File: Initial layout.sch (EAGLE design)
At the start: 53 parts, among them J1 502585-0470, U2 TPS54540DDARQ1

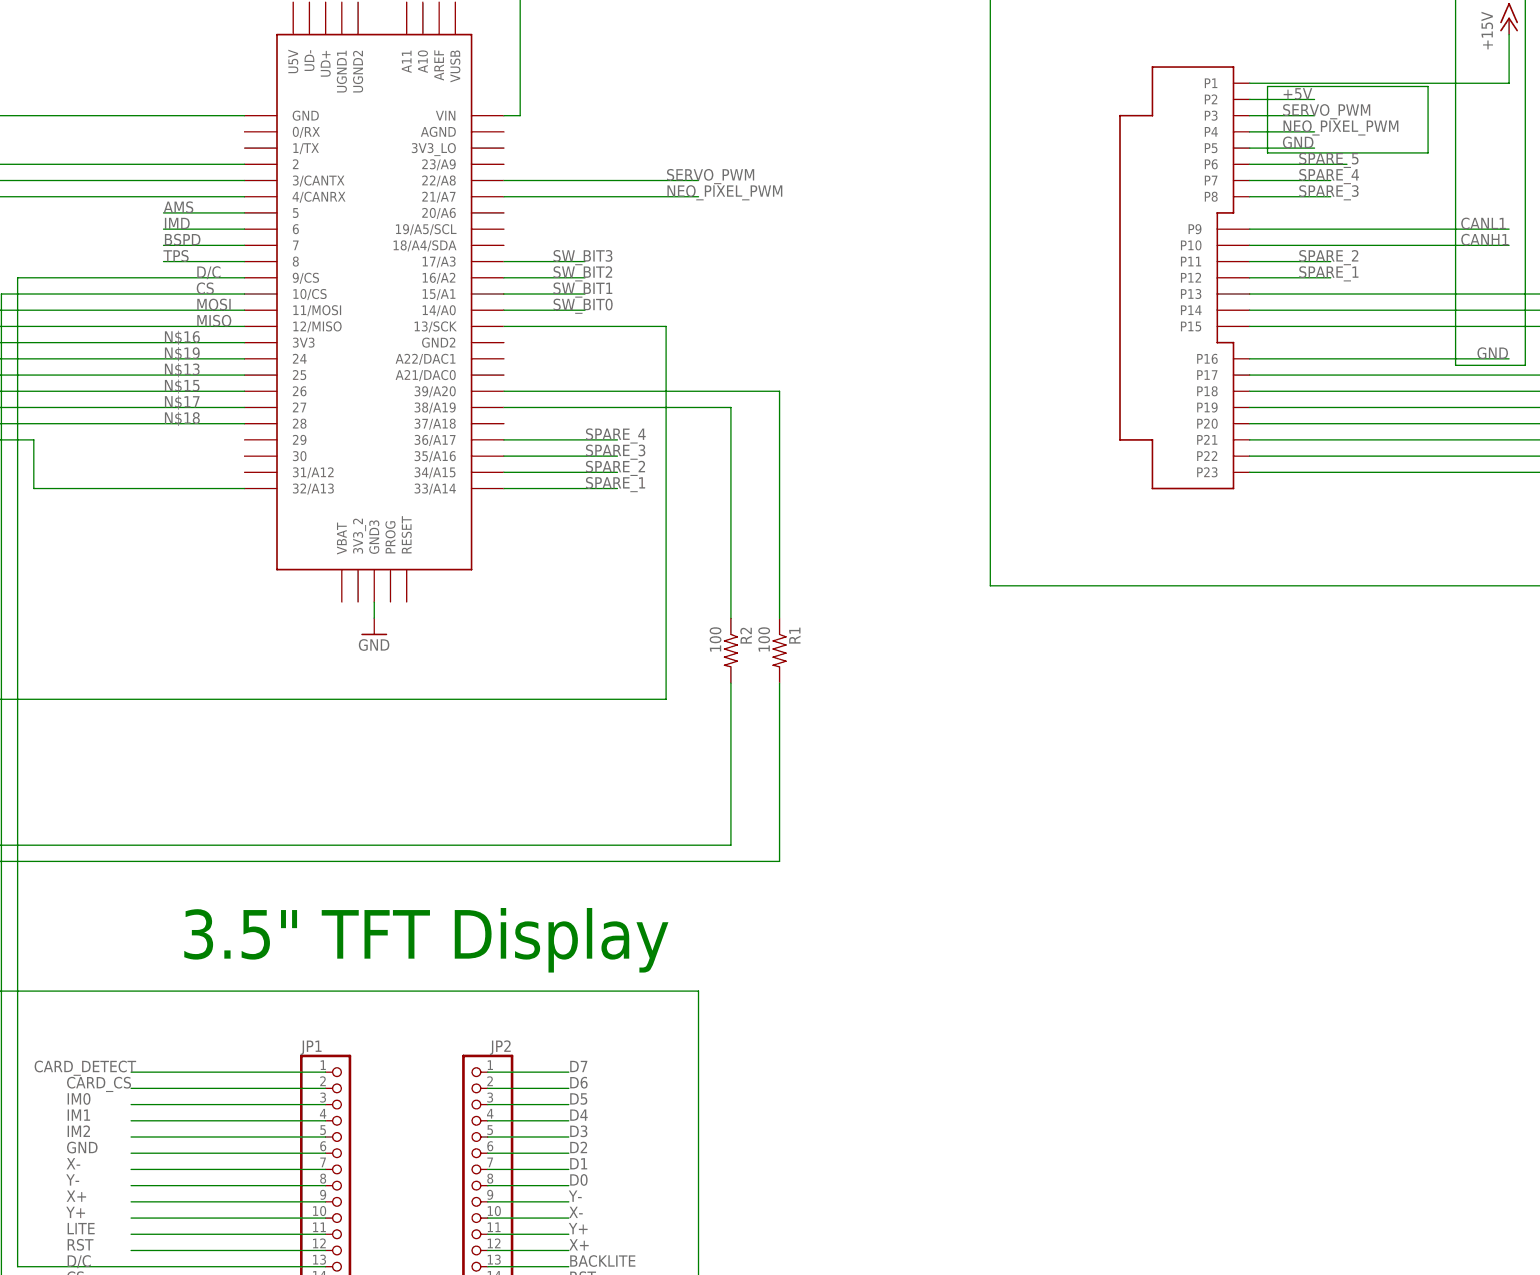
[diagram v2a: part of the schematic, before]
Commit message: Defined Pins, Updated names on schematic
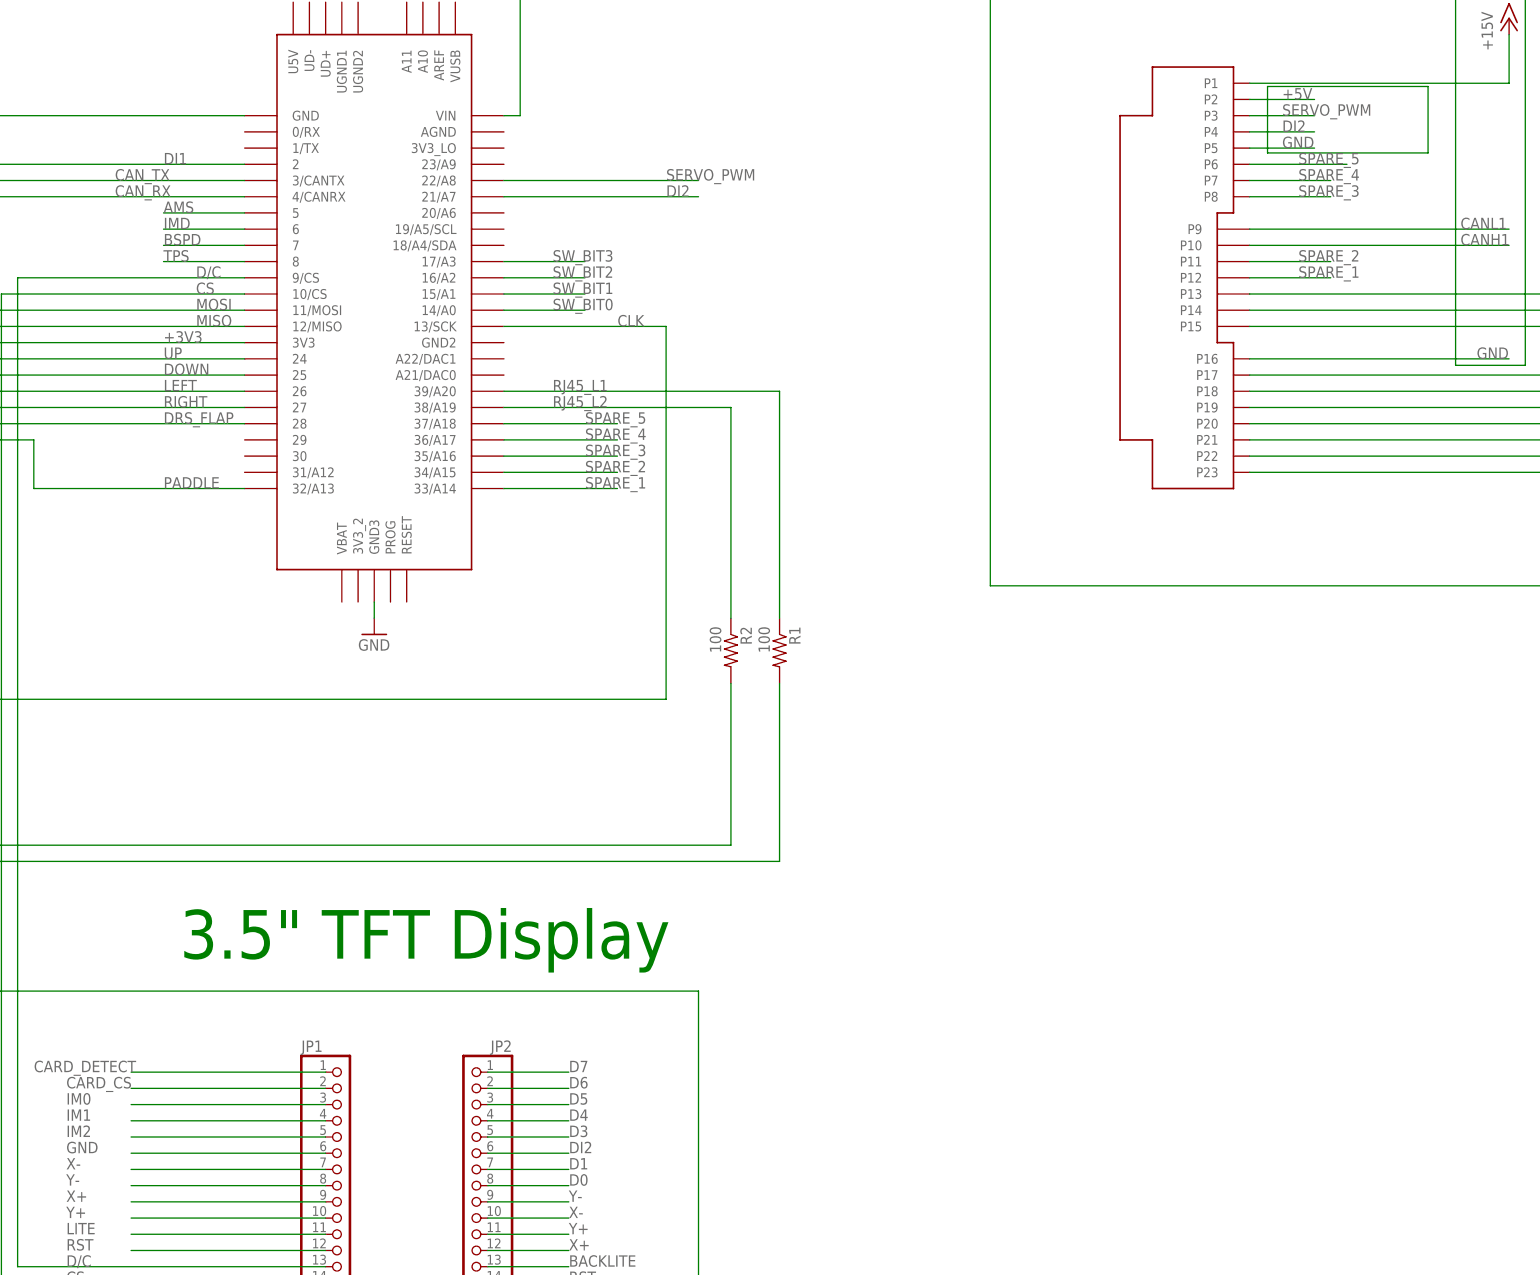
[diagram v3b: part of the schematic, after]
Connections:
- net N$13 renamed DOWN
- net N$15 renamed LEFT
- net N$17 renamed RIGHT
- net N$18 renamed DRS_FLAP
- net N$19 renamed UP
- net N$26 renamed CAN_RX
- net N$27 renamed DI1
- net N$28 renamed CAN_TX
- net N$3 renamed PADDLE
- net N$41 renamed RJ45_L1
- net N$42 renamed RJ45_L2
- removed net D2: JP2.6
- removed net N$16: U$2.3V3
- removed net NEO_PIXEL_PWM: U$1.P4, U$2.21/A7
- new net DI2: JP2.6, U$1.P4, U$2.21/A7
- net +3V3: now also U$2.3V3
- net SPARE_5: now also U$2.37/A18
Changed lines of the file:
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@@
 <wire x1="299.72" y1="-314.96" x2="187.96" y2="-314.96" width="0.1524" layer="91"/>
 <wire x1="187.96" y1="-314.96" x2="187.96" y2="-414.02" width="0.1524" layer="91"/>
+<label x="292.1" y="-256.54" size="1.778" layer="95"/>
 </segment>
 </net>
@@
 </segment>
 </net>
-<net name="D2" class="0">
+<net name="DI2" class="0">
 <segment>
 <pinref part="JP2" gate="A" pin="6"/>
 <wire x1="271.78" y1="-386.08" x2="284.48" y2="-386.08" width="0.1524" layer="91"/>
 <label x="284.48" y="-386.08" size="1.778" layer="95"/>
+</segment>
+<segment>
+<pinref part="U$1" gate="G$1" pin="P4"/>
+<wire x1="391.16" y1="-226.06" x2="401.32" y2="-226.06" width="0.1524" layer="91"/>
+<label x="396.24" y="-226.06" size="1.778" layer="95"/>
+</segment>
+<segment>
+<pinref part="U$2" gate="G$1" pin="21/A7"/>
+<wire x1="274.32" y1="-236.22" x2="304.8" y2="-236.22" width="0.1524" layer="91"/>
+<label x="299.72" y="-236.22" size="1.778" layer="95"/>
 </segment>
 </net>
@@
 <junction x="45.72" y="-391.16"/>
 </segment>
-</net>
-<net name="N$13" class="0">
+<segment>
+<pinref part="U$2" gate="G$1" pin="3V3"/>
+<wire x1="137.3124" y1="-259.08" x2="233.68" y2="-259.08" width="0.1524" layer="91"/>
+<label x="220.98" y="-259.08" size="1.778" layer="95"/>
+</segment>
+</net>
+<net name="DOWN" class="0">
 <segment>
 <pinref part="U$2" gate="G$1" pin="25"/>
@@
 </segment>
 </net>
-<net name="N$15" class="0">
+<net name="LEFT" class="0">
 <segment>
 <pinref part="U$2" gate="G$1" pin="26"/>
@@
 </segment>
 </net>
-<net name="N$17" class="0">
+<net name="RIGHT" class="0">
 <segment>
 <pinref part="U$2" gate="G$1" pin="27"/>
@@
 </segment>
 </net>
-<net name="N$18" class="0">
+<net name="DRS_FLAP" class="0">
 <segment>
 <pinref part="U$2" gate="G$1" pin="28"/>
@@
 </segment>
 </net>
-<net name="N$3" class="0">
+<net name="PADDLE" class="0">
 <segment>
 <wire x1="200.66" y1="-274.32" x2="200.66" y2="-281.94" width="0.1524" layer="91"/>
@@
 <pinref part="U$2" gate="G$1" pin="32/A13"/>
 <wire x1="233.68" y1="-281.94" x2="200.66" y2="-281.94" width="0.1524" layer="91"/>
+<label x="220.98" y="-281.94" size="1.778" layer="95"/>
 </segment>
 </net>
@@
 </segment>
 </net>
-<net name="N$16" class="0">
-<segment>
-<pinref part="U$2" gate="G$1" pin="3V3"/>
-<wire x1="137.3124" y1="-259.08" x2="233.68" y2="-259.08" width="0.1524" layer="91"/>
-<label x="220.98" y="-259.08" size="1.778" layer="95"/>
-</segment>
-</net>
-<net name="N$19" class="0">
+<net name="UP" class="0">
 <segment>
 <pinref part="U$2" gate="G$1" pin="24"/>
@@
 </segment>
 </net>
-<net name="N$28" class="0">
+<net name="CAN_TX" class="0">
 <segment>
 <pinref part="U3" gate="G$1" pin="TXD"/>
@@
 <wire x1="-10.16" y1="-375.92" x2="-10.16" y2="-233.68" width="0.1524" layer="91"/>
 <wire x1="-10.16" y1="-233.68" x2="233.68" y2="-233.68" width="0.1524" layer="91"/>
-</segment>
-</net>
-<net name="N$26" class="0">
+<label x="213.36" y="-233.68" size="1.778" layer="95"/>
+</segment>
+</net>
+<net name="CAN_RX" class="0">
 <segment>
 <pinref part="U3" gate="G$1" pin="RXD"/>
@@
 <pinref part="U$2" gate="G$1" pin="4/CANRX"/>
 <wire x1="-7.62" y1="-236.22" x2="233.68" y2="-236.22" width="0.1524" layer="91"/>
+<label x="213.36" y="-236.22" size="1.778" layer="95"/>
 </segment>
 </net>
@@
 </segment>
 </net>
-<net name="N$27" class="0">
+<net name="DI1" class="0">
 <segment>
 <pinref part="U$2" gate="G$1" pin="2"/>
@@
 <pinref part="LED1" gate="G$1" pin="DI"/>
 <wire x1="-10.16" y1="-129.54" x2="30.48" y2="-129.54" width="0.1524" layer="91"/>
+<label x="220.98" y="-231.14" size="1.778" layer="95"/>
 </segment>
 </net>
@@
 </segment>
 </net>
-<net name="N$41" class="0">
+<net name="RJ45_L1" class="0">
 <segment>
 <pinref part="U$2" gate="G$1" pin="39/A20"/>
@@
 <wire x1="317.5" y1="-302.26" x2="317.5" y2="-266.7" width="0.1524" layer="91"/>
 <wire x1="317.5" y1="-266.7" x2="274.32" y2="-266.7" width="0.1524" layer="91"/>
-</segment>
-</net>
-<net name="N$42" class="0">
+<label x="281.94" y="-266.7" size="1.778" layer="95"/>
+</segment>
+</net>
+<net name="RJ45_L2" class="0">
 <segment>
 <pinref part="U$2" gate="G$1" pin="38/A19"/>
@@
 <wire x1="309.88" y1="-302.26" x2="309.88" y2="-269.24" width="0.1524" layer="91"/>
 <wire x1="309.88" y1="-269.24" x2="274.32" y2="-269.24" width="0.1524" layer="91"/>
-</segment>
-</net>
-<net name="NEO_PIXEL_PWM" class="0">
-<segment>
-<pinref part="U$1" gate="G$1" pin="P4"/>
-<wire x1="391.16" y1="-226.06" x2="401.32" y2="-226.06" width="0.1524" layer="91"/>
-<label x="396.24" y="-226.06" size="1.778" layer="95"/>
-</segment>
-<segment>
-<pinref part="U$2" gate="G$1" pin="21/A7"/>
-<wire x1="274.32" y1="-236.22" x2="304.8" y2="-236.22" width="0.1524" layer="91"/>
-<label x="299.72" y="-236.22" size="1.778" layer="95"/>
+<label x="281.94" y="-269.24" size="1.778" layer="95"/>
 </segment>
 </net>
@@
 <label x="398.78" y="-231.14" size="1.778" layer="95"/>
 </segment>
-</net>
+<segment>
+<pinref part="U$2" gate="G$1" pin="37/A18"/>
+<wire x1="274.32" y1="-271.78" x2="292.1" y2="-271.78" width="0.1524" layer="91"/>
+<label x="287.02" y="-271.78" size="1.778" layer="95"/>
+</segment>
+</net>

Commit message: Updated schematic and board layout
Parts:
- added H2, H3: 5025840870, FormE:MOLEX_CLICKMATE-8-VERTICAL
- JP1: device adafruit:PINHD-1X20 -> pinhead:PINHD-1X8
- JP2: device adafruit:PINHD-1X20 -> pinhead:PINHD-1X1
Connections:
- removed net BACKLITE: JP2.13
- removed net C/D: JP2.17
- removed net CARD_CS: JP1.2
- removed net CARD_DETECT: JP1.1
- removed net D0: JP2.8
- removed net D1: JP2.7
- removed net D3: JP2.5
- removed net D4: JP2.4
- removed net D5: JP2.3
- removed net D6: JP2.2
- removed net D7: JP2.1
- removed net IM0: JP1.3
- removed net IM1: JP1.4
- removed net IM2: JP1.5
- removed net LITE: JP1.11
- removed net RD: JP2.15
- removed net RST: JP1.12, JP2.14
- removed net WR: JP2.16
- removed net X+: JP1.9, JP2.12
- removed net X-: JP1.7, JP2.10
- removed net Y+: JP1.10, JP2.11
- removed net Y-: JP1.8, JP2.9
- new net N$13: H3.2, JP1.2
- new net N$15: H3.3, JP1.3
- new net N$16: H3.4, JP1.4
- new net N$17: H3.5, JP1.5
- new net N$18: H3.6, JP1.6
- new net N$19: H3.7, JP1.7
- new net N$26: H3.8, JP1.8
- new net N$27: H2.6, JP2.1
- new net N$3: H3.1, JP1.1
- net +5V: now also H2.7; no longer JP1.19
- net CLK: now also H2.5; no longer JP1.17
- net CS: now also H2.2; no longer JP1.14, JP2.18
- net D/C: now also H2.1; no longer JP1.13
- net DI2: no longer JP2.6
- net GND: now also H2.8; no longer JP1.20, JP1.6, JP2.20
- net MISO: now also H2.4; no longer JP1.16
- net MOSI: now also H2.3; no longer JP1.15

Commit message: Finish board layout for main dash
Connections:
- net CANH1 renamed CAN_P
- net CANL1 renamed CAN_N
- removed net N$11: H1.1
- removed net N$20: H1.2
- removed net N$21: H1.3
- removed net N$22: H1.4
- removed net N$23: H1.5
- removed net N$24: H1.6
- net +3V3: now also H1.1
- net DOWN: now also H1.3
- net DRS_FLAP: now also H1.6
- net LEFT: now also H1.4
- net RIGHT: now also H1.5
- net UP: now also H1.2
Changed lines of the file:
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@@
 <?xml version="1.0" encoding="utf-8"?>
 <!DOCTYPE eagle SYSTEM "eagle.dtd">
-<eagle version="8.6.0">
+<eagle version="8.5.0">
 <drawing>
 <settings>
@@
 </segment>
 <segment>
+<pinref part="H1" gate="G$1" pin="1"/>
+<wire x1="129.54" y1="-378.46" x2="101.6" y2="-378.46" width="0.1524" layer="91"/>
+<wire x1="101.6" y1="-378.46" x2="101.6" y2="-259.08" width="0.1524" layer="91"/>
 <pinref part="U$2" gate="G$1" pin="3V3"/>
-<wire x1="137.3124" y1="-259.08" x2="233.68" y2="-259.08" width="0.1524" layer="91"/>
-<label x="220.98" y="-259.08" size="1.778" layer="95"/>
-</segment>
-</net>
-<net name="DOWN" class="0">
-<segment>
-<pinref part="U$2" gate="G$1" pin="25"/>
-<wire x1="233.68" y1="-264.16" x2="132.2324" y2="-264.16" width="0.1524" layer="91"/>
-<label x="220.98" y="-264.16" size="1.778" layer="95"/>
-</segment>
-</net>
-<net name="LEFT" class="0">
-<segment>
-<pinref part="U$2" gate="G$1" pin="26"/>
-<wire x1="233.68" y1="-266.7" x2="129.6924" y2="-266.7" width="0.1524" layer="91"/>
-<label x="220.98" y="-266.7" size="1.778" layer="95"/>
-</segment>
-</net>
-<net name="RIGHT" class="0">
-<segment>
-<pinref part="U$2" gate="G$1" pin="27"/>
-<wire x1="233.68" y1="-269.24" x2="127.1524" y2="-269.24" width="0.1524" layer="91"/>
-<label x="220.98" y="-269.24" size="1.778" layer="95"/>
-</segment>
-</net>
-<net name="DRS_FLAP" class="0">
-<segment>
-<pinref part="U$2" gate="G$1" pin="28"/>
-<wire x1="233.68" y1="-271.78" x2="124.6124" y2="-271.78" width="0.1524" layer="91"/>
-<label x="220.98" y="-271.78" size="1.778" layer="95"/>
-</segment>
-</net>
-<net name="CANL1" class="0">
+<wire x1="233.68" y1="-259.08" x2="101.6" y2="-259.08" width="0.1524" layer="91"/>
+<label x="218.44" y="-259.08" size="1.778" layer="95"/>
+</segment>
+</net>
+<net name="CAN_N" class="0">
 <segment>
 <pinref part="U3" gate="G$1" pin="CANL"/>
@@
 <pinref part="U$2" gate="G$1" pin="32/A13"/>
 <wire x1="233.68" y1="-281.94" x2="200.66" y2="-281.94" width="0.1524" layer="91"/>
-<label x="220.98" y="-281.94" size="1.778" layer="95"/>
+<label x="218.44" y="-281.94" size="1.778" layer="95"/>
 </segment>
 </net>
@@
 <net name="UP" class="0">
 <segment>
-<pinref part="U$2" gate="G$1" pin="24"/>
-<wire x1="233.68" y1="-261.62" x2="134.7724" y2="-261.62" width="0.1524" layer="91"/>
-<label x="220.98" y="-261.62" size="1.778" layer="95"/>
-</segment>
-</net>
-<net name="N$11" class="0">
-<segment>
-<pinref part="H1" gate="G$1" pin="1"/>
-<wire x1="129.54" y1="-378.46" x2="101.6" y2="-378.46" width="0.1524" layer="91"/>
-<wire x1="101.6" y1="-378.46" x2="101.6" y2="-259.08" width="0.1524" layer="91"/>
-<wire x1="101.6" y1="-259.08" x2="137.16" y2="-259.08" width="0.1524" layer="91"/>
-</segment>
-</net>
-<net name="N$20" class="0">
-<segment>
 <pinref part="H1" gate="G$1" pin="2"/>
 <wire x1="129.54" y1="-381" x2="99.06" y2="-381" width="0.1524" layer="91"/>
 <wire x1="99.06" y1="-381" x2="99.06" y2="-261.62" width="0.1524" layer="91"/>
-<wire x1="99.06" y1="-261.62" x2="134.62" y2="-261.62" width="0.1524" layer="91"/>
-</segment>
-</net>
-<net name="N$21" class="0">
+<pinref part="U$2" gate="G$1" pin="24"/>
+<wire x1="99.06" y1="-261.62" x2="233.68" y2="-261.62" width="0.1524" layer="91"/>
+<label x="218.44" y="-261.62" size="1.778" layer="95"/>
+</segment>
+</net>
+<net name="DOWN" class="0">
 <segment>
 <pinref part="H1" gate="G$1" pin="3"/>
 <wire x1="129.54" y1="-383.54" x2="96.52" y2="-383.54" width="0.1524" layer="91"/>
 <wire x1="96.52" y1="-383.54" x2="96.52" y2="-264.16" width="0.1524" layer="91"/>
-<wire x1="96.52" y1="-264.16" x2="132.08" y2="-264.16" width="0.1524" layer="91"/>
-</segment>
-</net>
-<net name="N$22" class="0">
+<pinref part="U$2" gate="G$1" pin="25"/>
+<wire x1="233.68" y1="-264.16" x2="96.52" y2="-264.16" width="0.1524" layer="91"/>
+<label x="218.44" y="-264.16" size="1.778" layer="95"/>
+</segment>
+</net>
+<net name="LEFT" class="0">
 <segment>
 <pinref part="H1" gate="G$1" pin="4"/>
 <wire x1="129.54" y1="-386.08" x2="93.98" y2="-386.08" width="0.1524" layer="91"/>
 <wire x1="93.98" y1="-386.08" x2="93.98" y2="-266.7" width="0.1524" layer="91"/>
-<wire x1="93.98" y1="-266.7" x2="129.54" y2="-266.7" width="0.1524" layer="91"/>
-</segment>
-</net>
-<net name="N$23" class="0">
+<pinref part="U$2" gate="G$1" pin="26"/>
+<wire x1="93.98" y1="-266.7" x2="233.68" y2="-266.7" width="0.1524" layer="91"/>
+<label x="218.44" y="-266.7" size="1.778" layer="95"/>
+</segment>
+</net>
+<net name="RIGHT" class="0">
 <segment>
 <pinref part="H1" gate="G$1" pin="5"/>
 <wire x1="129.54" y1="-388.62" x2="91.44" y2="-388.62" width="0.1524" layer="91"/>
 <wire x1="91.44" y1="-388.62" x2="91.44" y2="-269.24" width="0.1524" layer="91"/>
-<wire x1="91.44" y1="-269.24" x2="127" y2="-269.24" width="0.1524" layer="91"/>
-</segment>
-</net>
-<net name="N$24" class="0">
+<pinref part="U$2" gate="G$1" pin="27"/>
+<wire x1="233.68" y1="-269.24" x2="91.44" y2="-269.24" width="0.1524" layer="91"/>
+<label x="218.44" y="-269.24" size="1.778" layer="95"/>
+</segment>
+</net>
+<net name="DRS_FLAP" class="0">
 <segment>
 <pinref part="H1" gate="G$1" pin="6"/>
 <wire x1="129.54" y1="-391.16" x2="88.9" y2="-391.16" width="0.1524" layer="91"/>
 <wire x1="88.9" y1="-391.16" x2="88.9" y2="-271.78" width="0.1524" layer="91"/>
-<wire x1="88.9" y1="-271.78" x2="124.46" y2="-271.78" width="0.1524" layer="91"/>
-</segment>
-</net>
-<net name="CANH1" class="0">
+<pinref part="U$2" gate="G$1" pin="28"/>
+<wire x1="88.9" y1="-271.78" x2="233.68" y2="-271.78" width="0.1524" layer="91"/>
+<label x="218.44" y="-271.78" size="1.778" layer="95"/>
+</segment>
+</net>
+<net name="CAN_P" class="0">
 <segment>
 <pinref part="R4" gate="G$1" pin="1"/>
